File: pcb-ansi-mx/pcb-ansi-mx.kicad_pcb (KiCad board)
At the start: 2 copper layers, 200 parts, among them J1 USB_C_Receptacle_USB2.0, J2 Conn_01x04, J3 Conn_01x05, SW1 SW_Push, SW2 SW_Push, U1 XC6206PxxxMR, U2 SRV05-4, U3 RP2040, U4 W25Q128JVS, Y1 Crystal_GND24

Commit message: feat: add rotary encoder
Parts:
- added ENC1: RotaryEncoder_Switch, PCM_marbastlib-various:ROT_Alps_EC11E-Switch, F.Cu at (319.1, 23.8)

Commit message: feat: initial key matrix + encoder debounce
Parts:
- added C13: 22p, Capacitor_SMD:C_0402_1005Metric, B.Cu at (191.3, 166.3)
- added C14: 22p, Capacitor_SMD:C_0402_1005Metric, B.Cu at (191.3, 168.3)
- added D_ENC1: D_Small, Diode_SMD:D_SOD-123, B.Cu at (307.2, 23.8)
- added R10: 5k1, Resistor_SMD:R_0402_1005Metric, B.Cu at (343.2, 24.6)
- added R11: 27, Resistor_SMD:R_0402_1005Metric, B.Cu at (194.2, 165.0)
- added R12: 27, Resistor_SMD:R_0402_1005Metric, B.Cu at (194.2, 166.9)
- added R13: 1k, Resistor_SMD:R_0402_1005Metric, B.Cu at (194.2, 168.9)
- C10: value 1u -> 10n
- C11: value 22p -> 10n
- C12: value 22p -> 1u
- ENC1: moved to B.Cu
- R7, R8: value 27 -> 5k1
- R9: value 1k -> 5k1
- S1: value Backspace -> LShift; footprint PCM_marbastlib-mx:STAB_MX_P_2u -> PCM_marbastlib-mx:STAB_MX_P_2.25u; moved to B.Cu
- S2: value Enter -> Space; footprint PCM_marbastlib-mx:STAB_MX_P_2.25u -> PCM_marbastlib-mx:STAB_MX_P_6.25u; moved to B.Cu
- S3: value LShift -> Backspace; footprint PCM_marbastlib-mx:STAB_MX_P_2.25u -> PCM_marbastlib-mx:STAB_MX_P_2u; moved to B.Cu
- S4: value Space -> Enter; footprint PCM_marbastlib-mx:STAB_MX_P_6.25u -> PCM_marbastlib-mx:STAB_MX_P_2.25u; moved to B.Cu
- moved R9 329.1 mm to (346.1, 24.6)
- moved R7 328.6 mm to (346.4, 22.2)
- moved R8 327.1 mm to (343.8, 22.2)
- moved C10 265.8 mm to (353.5, 22.2)
- moved C11 265.8 mm to (353.5, 24.2)
- moved S1 252.4 mm to (34.9, 104.0), turned to 180 degrees
- moved S3 251.2 mm to (280.2, 46.8), turned to 180 degrees
- moved S2 139.2 mm to (144.5, 123.0)
- moved S4 138.1 mm to (277.8, 84.9)
- moved J1 52.2 mm to (77.3, 159.3)
- moved C1 13.9 mm to (122.8, 170.5)
- moved C2 13.9 mm to (122.8, 172.5)
- moved C3 13.9 mm to (122.8, 174.5)
- moved C4 13.9 mm to (122.8, 176.4)
- moved C5 13.9 mm to (43.4, 178.7)
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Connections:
- C10 pad 1: +3V3 -> ENC_B
- C11 pad 1: GND -> ENC_A
- C11 pad 2: XIN -> GND
- C12 pad 1: GND -> +3V3
- C12 pad 2: Net-(C12-Pad2) -> GND
- D1 pad 1: unconnected-(D1-K-Pad1) -> ROW0
- D10 pad 1: unconnected-(D10-K-Pad1) -> ROW0
- D11 pad 1: unconnected-(D11-K-Pad1) -> ROW0
- D12 pad 1: unconnected-(D12-K-Pad1) -> ROW0
- D13 pad 1: unconnected-(D13-K-Pad1) -> ROW0
- D14 pad 1: unconnected-(D14-K-Pad1) -> ROW0
- D15 pad 1: unconnected-(D15-K-Pad1) -> ROW1
- D16 pad 1: unconnected-(D16-K-Pad1) -> ROW1
- D17 pad 1: unconnected-(D17-K-Pad1) -> ROW1
- D18 pad 1: unconnected-(D18-K-Pad1) -> ROW1
- D19 pad 1: unconnected-(D19-K-Pad1) -> ROW1
- D2 pad 1: unconnected-(D2-K-Pad1) -> ROW0
- D20 pad 1: unconnected-(D20-K-Pad1) -> ROW1
- D21 pad 1: unconnected-(D21-K-Pad1) -> ROW1
- D22 pad 1: unconnected-(D22-K-Pad1) -> ROW1
- D23 pad 1: unconnected-(D23-K-Pad1) -> ROW1
- D24 pad 1: unconnected-(D24-K-Pad1) -> ROW1
- D25 pad 1: unconnected-(D25-K-Pad1) -> ROW1
- D26 pad 1: unconnected-(D26-K-Pad1) -> ROW1
- D27 pad 1: unconnected-(D27-K-Pad1) -> ROW1
- D28 pad 1: unconnected-(D28-K-Pad1) -> ROW1
- D29 pad 1: unconnected-(D29-K-Pad1) -> ROW1
- D3 pad 1: unconnected-(D3-K-Pad1) -> ROW0
- D30 pad 1: unconnected-(D30-K-Pad1) -> ROW2
- D31 pad 1: unconnected-(D31-K-Pad1) -> ROW2
- D32 pad 1: unconnected-(D32-K-Pad1) -> ROW2
- D33 pad 1: unconnected-(D33-K-Pad1) -> ROW2
- D34 pad 1: unconnected-(D34-K-Pad1) -> ROW2
- D35 pad 1: unconnected-(D35-K-Pad1) -> ROW2
- D36 pad 1: unconnected-(D36-K-Pad1) -> ROW2
- D37 pad 1: unconnected-(D37-K-Pad1) -> ROW2
- D38 pad 1: unconnected-(D38-K-Pad1) -> ROW2
- D39 pad 1: unconnected-(D39-K-Pad1) -> ROW2
- D4 pad 1: unconnected-(D4-K-Pad1) -> ROW0
- D40 pad 1: unconnected-(D40-K-Pad1) -> ROW2
- D41 pad 1: unconnected-(D41-K-Pad1) -> ROW2
- D42 pad 1: unconnected-(D42-K-Pad1) -> ROW2
- D43 pad 1: unconnected-(D43-K-Pad1) -> ROW2
- D44 pad 1: unconnected-(D44-K-Pad1) -> ROW2
- D45 pad 1: unconnected-(D45-K-Pad1) -> ROW3
- D46 pad 1: unconnected-(D46-K-Pad1) -> ROW3
- D47 pad 1: unconnected-(D47-K-Pad1) -> ROW3
- D48 pad 1: unconnected-(D48-K-Pad1) -> ROW3
- D49 pad 1: unconnected-(D49-K-Pad1) -> ROW3
- D5 pad 1: unconnected-(D5-K-Pad1) -> ROW0
- D50 pad 1: unconnected-(D50-K-Pad1) -> ROW3
- D51 pad 1: unconnected-(D51-K-Pad1) -> ROW3
- D52 pad 1: unconnected-(D52-K-Pad1) -> ROW3
- D53 pad 1: unconnected-(D53-K-Pad1) -> ROW3
- D54 pad 1: unconnected-(D54-K-Pad1) -> ROW3
- D55 pad 1: unconnected-(D55-K-Pad1) -> ROW3
- D56 pad 1: unconnected-(D56-K-Pad1) -> ROW3
- D57 pad 1: unconnected-(D57-K-Pad1) -> ROW3
- D58 pad 1: unconnected-(D58-K-Pad1) -> ROW3
- D59 pad 1: unconnected-(D59-K-Pad1) -> ROW4
- D6 pad 1: unconnected-(D6-K-Pad1) -> ROW0
- D60 pad 1: unconnected-(D60-K-Pad1) -> ROW4
- D61 pad 1: unconnected-(D61-K-Pad1) -> ROW4
- D62 pad 1: unconnected-(D62-K-Pad1) -> ROW4
- D63 pad 1: unconnected-(D63-K-Pad1) -> ROW4
- D64 pad 1: unconnected-(D64-K-Pad1) -> ROW4
- D65 pad 1: unconnected-(D65-K-Pad1) -> ROW4
- D66 pad 1: unconnected-(D66-K-Pad1) -> ROW4
- D67 pad 1: unconnected-(D67-K-Pad1) -> ROW4
- D68 pad 1: unconnected-(D68-K-Pad1) -> ROW4
- D69 pad 1: unconnected-(D69-K-Pad1) -> ROW4
- D7 pad 1: unconnected-(D7-K-Pad1) -> ROW0
- D70 pad 1: unconnected-(D70-K-Pad1) -> ROW4
- D71 pad 1: unconnected-(D71-K-Pad1) -> ROW4
- D72 pad 1: unconnected-(D72-K-Pad1) -> ROW4
- D73 pad 1: unconnected-(D73-K-Pad1) -> ROW5
- D74 pad 1: unconnected-(D74-K-Pad1) -> ROW5
- D75 pad 1: unconnected-(D75-K-Pad1) -> ROW5
- D76 pad 1: unconnected-(D76-K-Pad1) -> ROW5
- D77 pad 1: unconnected-(D77-K-Pad1) -> ROW5
- D78 pad 1: unconnected-(D78-K-Pad1) -> ROW5
- D79 pad 1: unconnected-(D79-K-Pad1) -> ROW5
- D8 pad 1: unconnected-(D8-K-Pad1) -> ROW0
- D80 pad 1: unconnected-(D80-K-Pad1) -> ROW5
- D81 pad 1: unconnected-(D81-K-Pad1) -> ROW5
- D82 pad 1: unconnected-(D82-K-Pad1) -> ROW5
- D9 pad 1: unconnected-(D9-K-Pad1) -> ROW0
- ENC1 pad A: unconnected-(ENC1-PadA) -> Net-(ENC1-PadA)
- ENC1 pad B: unconnected-(ENC1-PadB) -> Net-(ENC1-PadB)
- ENC1 pad C: unconnected-(ENC1-PadC) -> GND
- ENC1 pad S1: unconnected-(ENC1-PadS1) -> Net-(D_ENC1-A)
- ENC1 pad S2: unconnected-(ENC1-PadS2) -> COL14
- MX1 pad 1: unconnected-(MX1-Pad1) -> COL0
- MX10 pad 1: unconnected-(MX10-Pad1) -> COL9
- MX11 pad 1: unconnected-(MX11-Pad1) -> COL10
- MX12 pad 1: unconnected-(MX12-Pad1) -> COL11
- MX13 pad 1: unconnected-(MX13-Pad1) -> COL12
- MX14 pad 1: unconnected-(MX14-Pad1) -> COL13
- MX15 pad 1: unconnected-(MX15-Pad1) -> COL0
- MX16 pad 1: unconnected-(MX16-Pad1) -> COL1
- MX17 pad 1: unconnected-(MX17-Pad1) -> COL2
- MX18 pad 1: unconnected-(MX18-Pad1) -> COL3
- MX19 pad 1: unconnected-(MX19-Pad1) -> COL4
- MX2 pad 1: unconnected-(MX2-Pad1) -> COL1
- MX20 pad 1: unconnected-(MX20-Pad1) -> COL5
- MX21 pad 1: unconnected-(MX21-Pad1) -> COL6
- MX22 pad 1: unconnected-(MX22-Pad1) -> COL7
- MX23 pad 1: unconnected-(MX23-Pad1) -> COL8
- MX24 pad 1: unconnected-(MX24-Pad1) -> COL9
- MX25 pad 1: unconnected-(MX25-Pad1) -> COL10
- MX26 pad 1: unconnected-(MX26-Pad1) -> COL11
- MX27 pad 1: unconnected-(MX27-Pad1) -> COL12
- MX28 pad 1: unconnected-(MX28-Pad1) -> COL13
- MX29 pad 1: unconnected-(MX29-Pad1) -> COL14
- MX3 pad 1: unconnected-(MX3-Pad1) -> COL2
- MX30 pad 1: unconnected-(MX30-Pad1) -> COL0
- MX31 pad 1: unconnected-(MX31-Pad1) -> COL1
- MX32 pad 1: unconnected-(MX32-Pad1) -> COL2
- MX33 pad 1: unconnected-(MX33-Pad1) -> COL3
- MX34 pad 1: unconnected-(MX34-Pad1) -> COL4
- MX35 pad 1: unconnected-(MX35-Pad1) -> COL5
- MX36 pad 1: unconnected-(MX36-Pad1) -> COL6
- MX37 pad 1: unconnected-(MX37-Pad1) -> COL7
- MX38 pad 1: unconnected-(MX38-Pad1) -> COL8
- MX39 pad 1: unconnected-(MX39-Pad1) -> COL9
- MX4 pad 1: unconnected-(MX4-Pad1) -> COL3
- MX40 pad 1: unconnected-(MX40-Pad1) -> COL10
- MX41 pad 1: unconnected-(MX41-Pad1) -> COL11
- MX42 pad 1: unconnected-(MX42-Pad1) -> COL12
- MX43 pad 1: unconnected-(MX43-Pad1) -> COL13
- MX44 pad 1: unconnected-(MX44-Pad1) -> COL14
- MX45 pad 1: unconnected-(MX45-Pad1) -> COL0
- MX46 pad 1: unconnected-(MX46-Pad1) -> COL1
- MX47 pad 1: unconnected-(MX47-Pad1) -> COL2
- MX48 pad 1: unconnected-(MX48-Pad1) -> COL3
- MX49 pad 1: unconnected-(MX49-Pad1) -> COL4
- MX5 pad 1: unconnected-(MX5-Pad1) -> COL4
- MX50 pad 1: unconnected-(MX50-Pad1) -> COL5
- MX51 pad 1: unconnected-(MX51-Pad1) -> COL6
- MX52 pad 1: unconnected-(MX52-Pad1) -> COL7
- MX53 pad 1: unconnected-(MX53-Pad1) -> COL8
- MX54 pad 1: unconnected-(MX54-Pad1) -> COL9
- MX55 pad 1: unconnected-(MX55-Pad1) -> COL10
- MX56 pad 1: unconnected-(MX56-Pad1) -> COL11
- MX57 pad 1: unconnected-(MX57-Pad1) -> COL12
- MX58 pad 1: unconnected-(MX58-Pad1) -> COL14
- MX59 pad 1: unconnected-(MX59-Pad1) -> COL0
- MX6 pad 1: unconnected-(MX6-Pad1) -> COL5
- MX60 pad 1: unconnected-(MX60-Pad1) -> COL1
- MX61 pad 1: unconnected-(MX61-Pad1) -> COL2
- MX62 pad 1: unconnected-(MX62-Pad1) -> COL3
- MX63 pad 1: unconnected-(MX63-Pad1) -> COL4
- MX64 pad 1: unconnected-(MX64-Pad1) -> COL5
- MX65 pad 1: unconnected-(MX65-Pad1) -> COL6
- MX66 pad 1: unconnected-(MX66-Pad1) -> COL7
- MX67 pad 1: unconnected-(MX67-Pad1) -> COL8
- MX68 pad 1: unconnected-(MX68-Pad1) -> COL9
- MX69 pad 1: unconnected-(MX69-Pad1) -> COL10
- MX7 pad 1: unconnected-(MX7-Pad1) -> COL6
- MX70 pad 1: unconnected-(MX70-Pad1) -> COL11
- MX71 pad 1: unconnected-(MX71-Pad1) -> COL12
- MX72 pad 1: unconnected-(MX72-Pad1) -> COL14
- MX73 pad 1: unconnected-(MX73-Pad1) -> COL0
- MX74 pad 1: unconnected-(MX74-Pad1) -> COL1
- MX75 pad 1: unconnected-(MX75-Pad1) -> COL2
- MX76 pad 1: unconnected-(MX76-Pad1) -> COL5
- MX77 pad 1: unconnected-(MX77-Pad1) -> COL8
- MX78 pad 1: unconnected-(MX78-Pad1) -> COL9
- MX79 pad 1: unconnected-(MX79-Pad1) -> COL10
- MX8 pad 1: unconnected-(MX8-Pad1) -> COL7
- MX80 pad 1: unconnected-(MX80-Pad1) -> COL11
- MX81 pad 1: unconnected-(MX81-Pad1) -> COL12
- MX82 pad 1: unconnected-(MX82-Pad1) -> COL13
- MX9 pad 1: unconnected-(MX9-Pad1) -> COL8
- R7 pad 1: D+ -> Net-(R7-Pad1)
- R7 pad 2: Net-(U3-USB_DP) -> Net-(ENC1-PadA)
- R8 pad 1: D- -> ENC_A
- R8 pad 2: Net-(U3-USB_DM) -> Net-(R7-Pad1)
- R9 pad 1: Net-(C12-Pad2) -> Net-(R10-Pad2)
- R9 pad 2: XOUT -> Net-(ENC1-PadB)
- Y1 pad 1: Net-(C12-Pad2) -> Net-(C14-Pad2)

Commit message: refactor: remove f13 (to make space for usb port)
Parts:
- removed D82: D_Small, Diode_SMD:D_SOD-123
- removed MX82: MX_SW_HS, PCM_marbastlib-mx:SW_MX_HS_1u
- MX29, MX42: footprint PCM_marbastlib-mx:SW_MX_HS_1u -> PCM_marbastlib-mx:SW_MX_HS_1.5u
- MX30, MX43: footprint PCM_marbastlib-mx:SW_MX_HS_1.5u -> PCM_marbastlib-mx:SW_MX_HS_1u
- MX44, MX69: footprint PCM_marbastlib-mx:SW_MX_HS_1u -> PCM_marbastlib-mx:SW_MX_HS_1.75u
- MX45, MX70: footprint PCM_marbastlib-mx:SW_MX_HS_1.75u -> PCM_marbastlib-mx:SW_MX_HS_1u
- MX72: footprint PCM_marbastlib-mx:SW_MX_HS_1u -> PCM_marbastlib-mx:SW_MX_HS_1.25u
- MX75: footprint PCM_marbastlib-mx:SW_MX_HS_1.25u -> PCM_marbastlib-mx:SW_MX_HS_1u
- moved MX29 291.1 mm to (27.8, 65.9)
- moved D29 291.1 mm to (31.0, 66.7)
- moved MX44 288.8 mm to (30.2, 84.9)
- moved D44 288.8 mm to (33.3, 85.7)
- moved MX58 284.0 mm to (34.9, 104.0)
- moved D58 284.0 mm to (38.1, 104.8)
- moved MX72 269.5 mm to (25.4, 123.0)
- moved D72 269.5 mm to (28.6, 123.8)
- moved MX14 267.8 mm to (23.0, 46.8)
- moved D14 267.8 mm to (26.2, 47.6)
- moved J1 145.4 mm to (42.1, 18.3)
- moved D75 71.4 mm to (147.6, 123.8)
- moved MX75 71.4 mm to (144.5, 123.0)
- moved D76 69.1 mm to (216.7, 123.8)
- moved MX76 69.1 mm to (213.5, 123.0)
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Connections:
- D14 pad 1: ROW0 -> ROW1
- D29 pad 1: ROW1 -> ROW2
- D44 pad 1: ROW2 -> ROW3
- D58 pad 1: ROW3 -> ROW4
- D72 pad 1: ROW4 -> ROW5
- MX14 pad 1: COL13 -> COL0
- MX15 pad 1: COL0 -> COL1
- MX16 pad 1: COL1 -> COL2
- MX17 pad 1: COL2 -> COL3
- MX18 pad 1: COL3 -> COL4
- MX19 pad 1: COL4 -> COL5
- MX20 pad 1: COL5 -> COL6
- MX21 pad 1: COL6 -> COL7
- MX22 pad 1: COL7 -> COL8
- MX23 pad 1: COL8 -> COL9
- MX24 pad 1: COL9 -> COL10
- MX25 pad 1: COL10 -> COL11
- MX26 pad 1: COL11 -> COL12
- MX27 pad 1: COL12 -> COL13
- MX28 pad 1: COL13 -> COL14
- MX29 pad 1: COL14 -> COL0
- MX30 pad 1: COL0 -> COL1
- MX31 pad 1: COL1 -> COL2
- MX32 pad 1: COL2 -> COL3
- MX33 pad 1: COL3 -> COL4
- MX34 pad 1: COL4 -> COL5
- MX35 pad 1: COL5 -> COL6
- MX36 pad 1: COL6 -> COL7
- MX37 pad 1: COL7 -> COL8
- MX38 pad 1: COL8 -> COL9
- MX39 pad 1: COL9 -> COL10
- MX40 pad 1: COL10 -> COL11
- MX41 pad 1: COL11 -> COL12
- MX42 pad 1: COL12 -> COL13
- MX43 pad 1: COL13 -> COL14
- MX44 pad 1: COL14 -> COL0
- MX45 pad 1: COL0 -> COL1
- MX46 pad 1: COL1 -> COL2
- MX47 pad 1: COL2 -> COL3
- MX48 pad 1: COL3 -> COL4
- MX49 pad 1: COL4 -> COL5
- MX50 pad 1: COL5 -> COL6
- MX51 pad 1: COL6 -> COL7
- MX52 pad 1: COL7 -> COL8
- MX53 pad 1: COL8 -> COL9
- MX54 pad 1: COL9 -> COL10
- MX55 pad 1: COL10 -> COL11
- MX56 pad 1: COL11 -> COL12
- MX57 pad 1: COL12 -> COL14
- MX58 pad 1: COL14 -> COL0
- MX59 pad 1: COL0 -> COL1
- MX60 pad 1: COL1 -> COL2
- MX61 pad 1: COL2 -> COL3
- MX62 pad 1: COL3 -> COL4
- MX63 pad 1: COL4 -> COL5
- MX64 pad 1: COL5 -> COL6
- MX65 pad 1: COL6 -> COL7
- MX66 pad 1: COL7 -> COL8
- MX67 pad 1: COL8 -> COL9
- MX68 pad 1: COL9 -> COL10
- MX69 pad 1: COL10 -> COL11
- MX70 pad 1: COL11 -> COL12
- MX71 pad 1: COL12 -> COL14
- MX72 pad 1: COL14 -> COL0
- MX73 pad 1: COL0 -> COL1
- MX74 pad 1: COL1 -> COL2
- MX75 pad 1: COL2 -> COL5
- MX76 pad 1: COL5 -> COL8
- MX77 pad 1: COL8 -> COL9
- MX78 pad 1: COL9 -> COL10
- MX79 pad 1: COL10 -> COL11
- MX80 pad 1: COL11 -> COL12
- MX81 pad 1: COL12 -> COL13

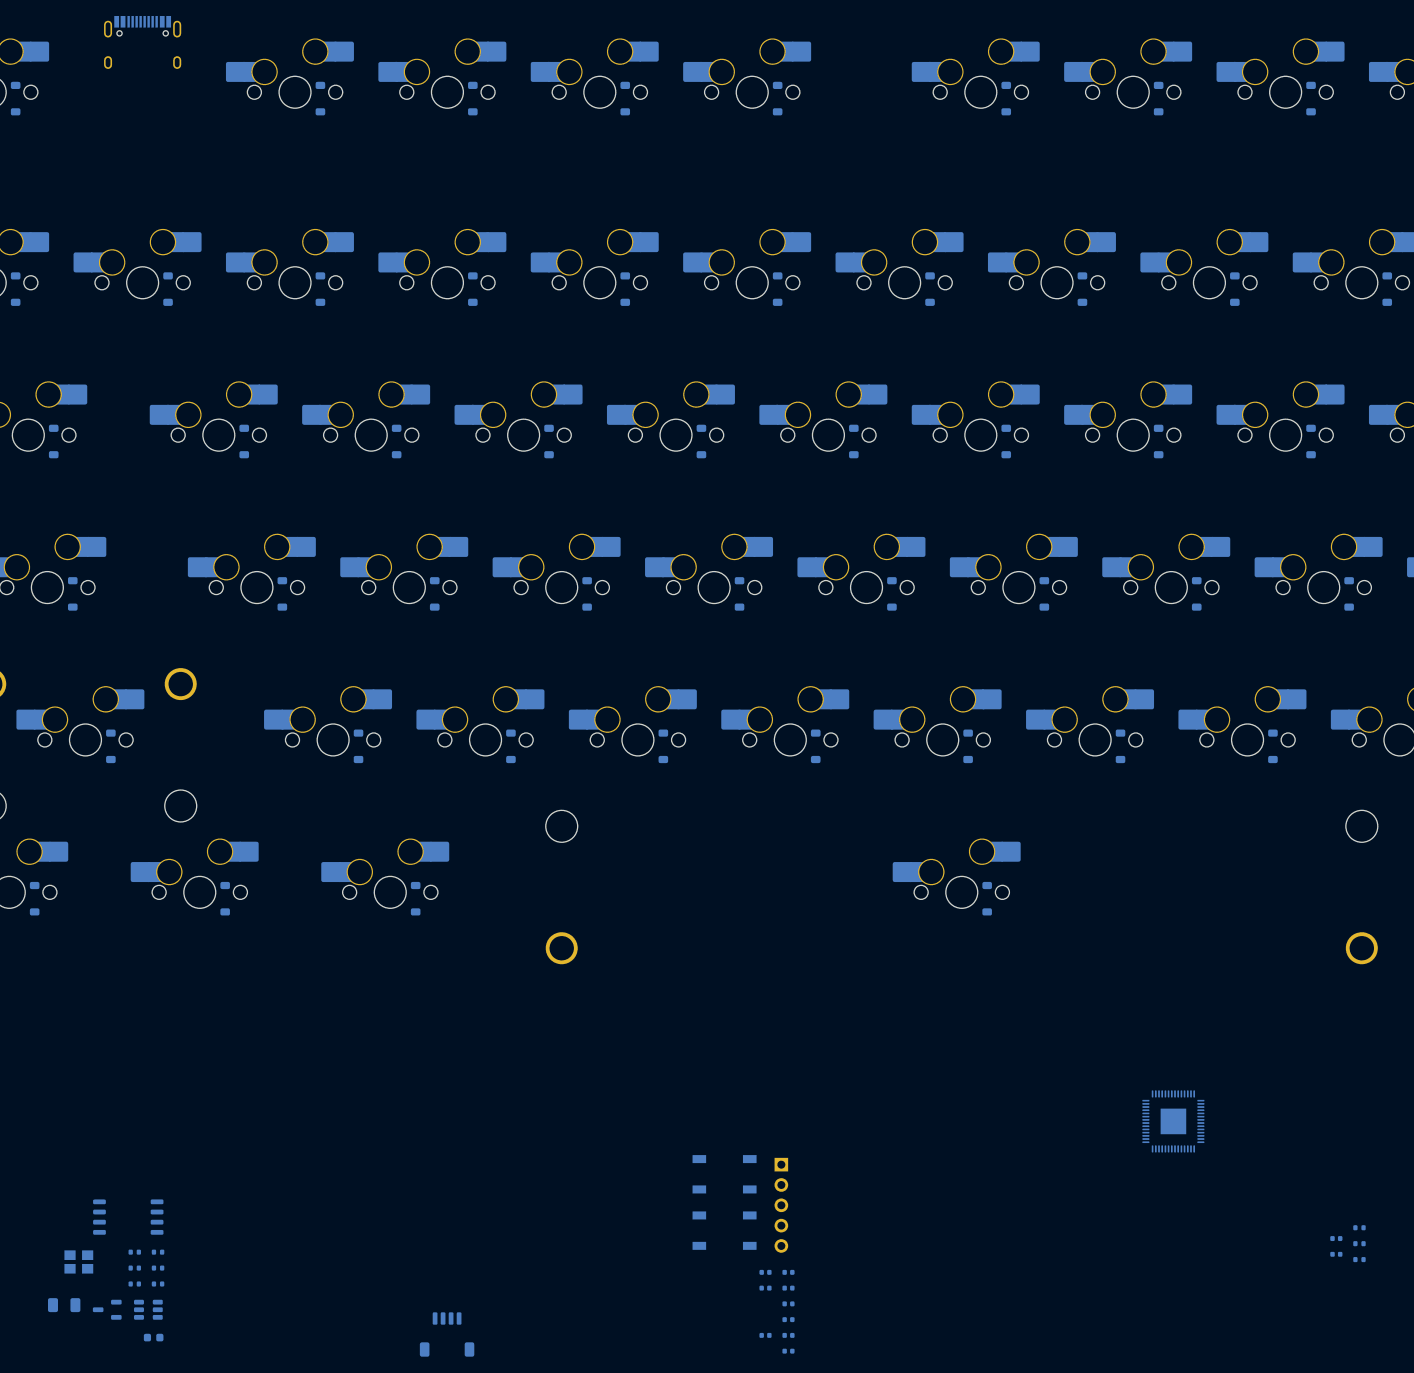
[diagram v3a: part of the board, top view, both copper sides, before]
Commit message: refactor: use molex instead of jst for daughterboard connector
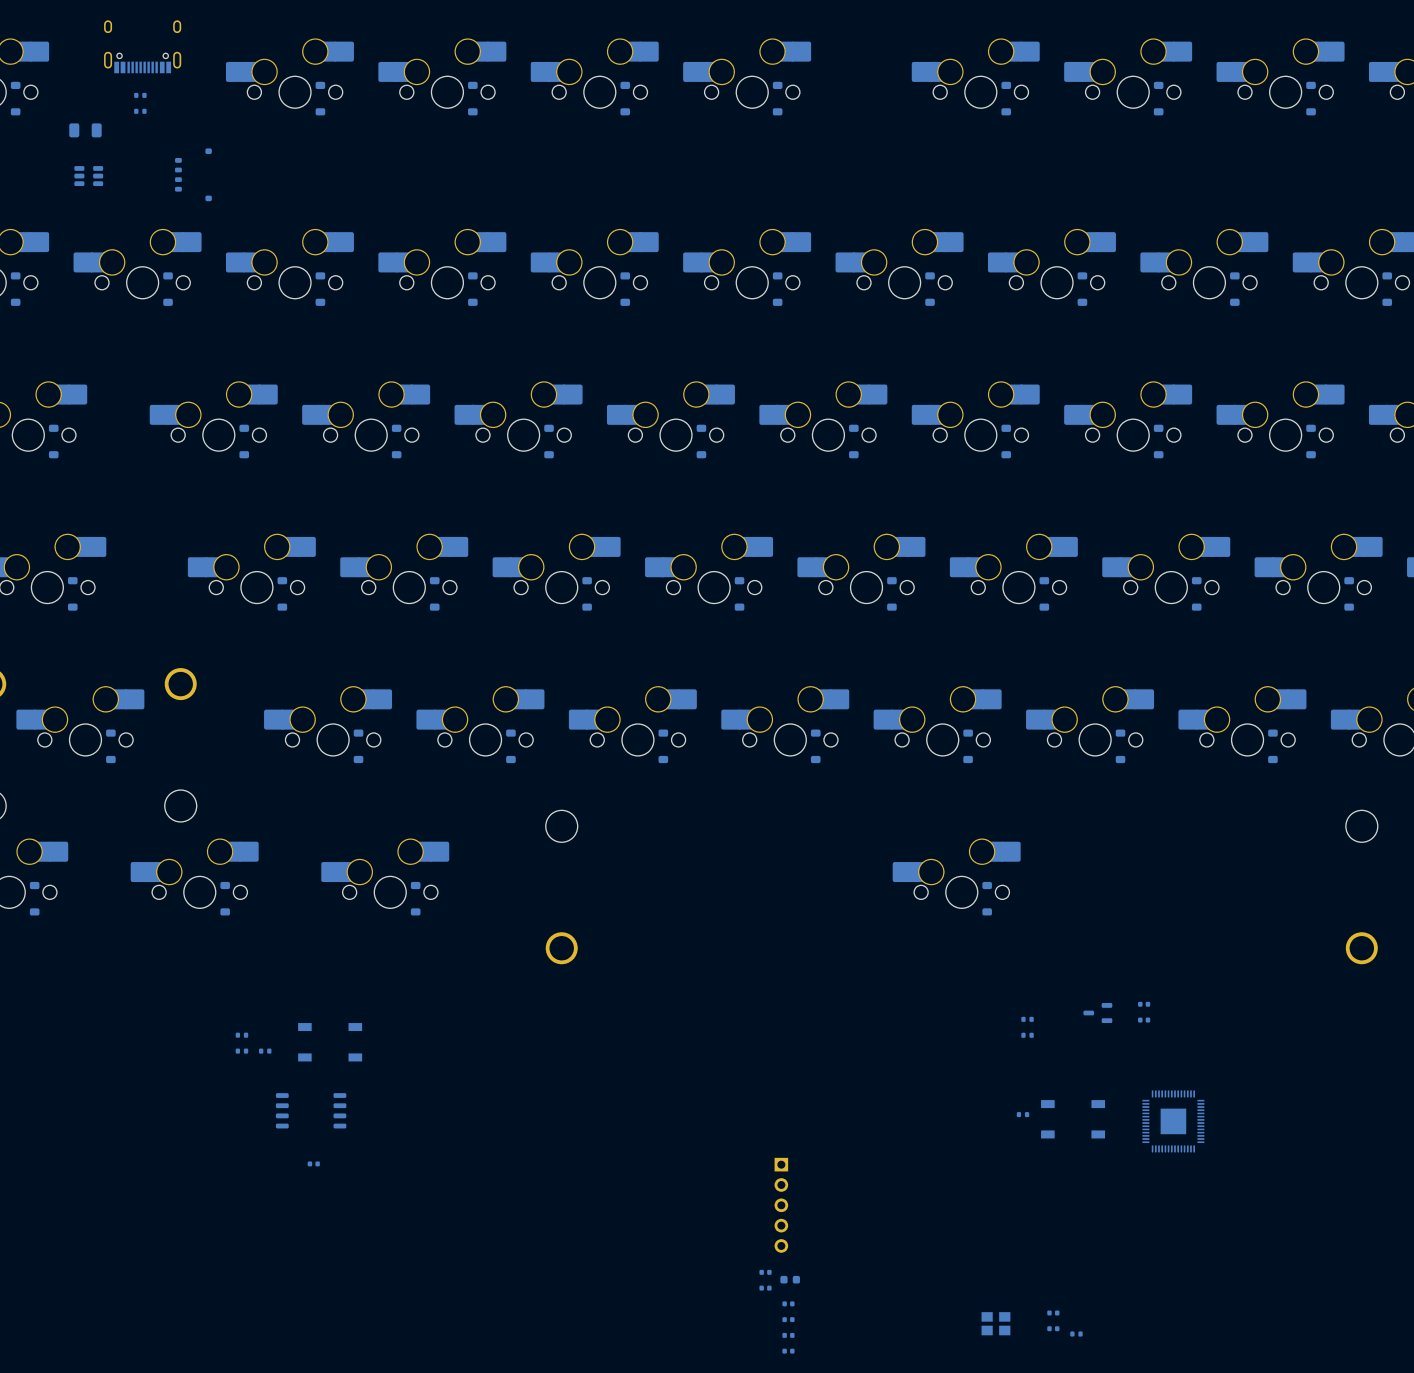
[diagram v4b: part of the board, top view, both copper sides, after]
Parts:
- J2: footprint Connector_JST:JST_SH_SM04B-SRSS-TB_1x04-1MP_P1.00mm_Horizontal -> Connector_Molex:Molex_Pico-EZmate_78171-0004_1x04-1MP_P1.20mm_Vertical
- moved J2 148.4 mm to (48.4, 33.3), turned to -90 degrees
- moved F1 146.9 mm to (34.9, 27.8)
- moved R1 144.6 mm to (41.8, 23.4)
- moved R2 144.6 mm to (41.8, 25.4)
- moved U2 141.9 mm to (35.3, 33.5)
- moved U1 129.3 mm to (161.5, 138.1)
- moved Y1 114.9 mm to (148.7, 176.9)
- moved R4 112.4 mm to (152.1, 150.8)
- moved C5 79.9 mm to (123.0, 171.4)
- moved C12 60.4 mm to (63.5, 157.0)
- moved C1 55.7 mm to (167.3, 137.0)
- moved C2 55.7 mm to (167.3, 139.0)
- moved SW2 54.6 mm to (65.5, 141.8)
- moved R11 49.0 mm to (152.7, 138.9)
- moved R12 49.0 mm to (152.7, 140.9)
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
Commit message: refactor: remove daughterboard connector
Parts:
- removed J2: Conn_01x04, Connector_Molex:Molex_Pico-EZmate_78171-0004_1x04-1MP_P1.20mm_Vertical
- added C15: 10n, Capacitor_SMD:C_0402_1005Metric, B.Cu at (330.5, 26.2)
- added C16: 1u, Capacitor_SMD:C_0402_1005Metric, B.Cu at (183.7, 138.1)
- added C17: 22p, Capacitor_SMD:C_0402_1005Metric, B.Cu at (172.6, 166.3)
- added C18: 22p, Capacitor_SMD:C_0402_1005Metric, B.Cu at (168.7, 166.3)
- C10, C11: value 10n -> 100n
- C12: value 1u -> 100n
- C13: value 22p -> 100n
- C14: value 22p -> 10n
- C5: value 10u -> 100n; footprint Capacitor_SMD:C_0603_1608Metric -> Capacitor_SMD:C_0402_1005Metric
- C6: value 1u -> 10u; footprint Capacitor_SMD:C_0402_1005Metric -> Capacitor_SMD:C_0603_1608Metric
- C7: value 100n -> 1u
- moved C14 233.6 mm to (331.4, 23.5), turned to 135 degrees
- moved C11 202.7 mm to (171.3, 146.0), turned to 90 degrees
- moved C10 201.7 mm to (176.7, 149.2), turned to 0 degrees
- moved R5 138.1 mm to (192.6, 142.1)
- moved R6 138.1 mm to (192.6, 144.1)
- moved SW2 138.1 mm to (203.6, 143.0)
- moved R3 138.1 mm to (195.5, 144.1)
- moved U4 117.3 mm to (180.2, 142.9)
- moved C12 107.1 mm to (170.6, 158.0), turned to -90 degrees
- moved C9 60.1 mm to (176.5, 152.4), turned to 0 degrees
- moved C5 55.4 mm to (172.2, 146.0), turned to 90 degrees
- moved C3 54.6 mm to (169.4, 146.0), turned to 90 degrees
- moved C6 54.5 mm to (161.9, 140.5)
- moved C7 52.1 mm to (164.6, 149.2)
- moved C4 50.1 mm to (169.4, 158.0), turned to -90 degrees
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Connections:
- C10 pad 1: ENC_B -> +3V3
- C11 pad 1: ENC_A -> +3V3
- C13 pad 1: GND -> +3V3
- C13 pad 2: XIN -> GND
- C14 pad 1: GND -> ENC_B
- C14 pad 2: Net-(C14-Pad2) -> GND
- C5 pad 1: +3V3 -> +1V1
- R13 pad 1: Net-(C14-Pad2) -> Net-(C18-Pad2)
- Y1 pad 1: Net-(C14-Pad2) -> Net-(C18-Pad2)
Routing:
- net D+: track 0.00 -> 3.19 mm
- net D-: track 0.00 -> 3.10 mm
- net Net-(J1-CC1): track 0.00 -> 2.77 mm
- net Net-(J1-CC2): track 0.00 -> 2.57 mm

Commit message: feat: route everything but encoder and matrix
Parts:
- ENC1: moved to F.Cu
- moved SW2 77.8 mm to (144.4, 92.6)
- moved R3 77.4 mm to (138.9, 91.3), turned to 0 degrees
- moved R6 73.1 mm to (138.9, 94.5)
- moved R5 72.8 mm to (138.9, 92.9)
- moved C1 70.4 mm to (102.7, 93.7), turned to 180 degrees
- moved U1 69.1 mm to (107.2, 95.2)
- moved C2 68.4 mm to (110.3, 95.2)
- moved C16 65.0 mm to (126.2, 107.9)
- moved C13 64.8 mm to (115.6, 111.2)
- moved C3 63.2 mm to (116.6, 111.2)
- moved C11 62.7 mm to (119.6, 110.6)
- moved C5 62.7 mm to (120.6, 110.6)
- moved R12 62.2 mm to (118.2, 108.6)
- moved R11 62.2 mm to (119.2, 108.6)
- moved R13 62.2 mm to (119.0, 125.8)
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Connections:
- J3 pad 1: RESET -> SWC
- J3 pad 2: +3V3 -> SWD
- J3 pad 3: GND -> RESET
- J3 pad 4: SWC -> +3V3
- J3 pad 5: SWD -> GND
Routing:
- net D+: track 3.19 -> 158.1 mm
- net D-: track 3.10 -> 156.5 mm
- net +3V3: track 0.00 -> 134.6 mm, vias 0 -> 4
- net +5V: track 0.00 -> 132.3 mm
- net GND: track 0.00 -> 129.8 mm, vias 0 -> 24
- net Q_SEL: track 0.00 -> 45.6 mm
- net +1V1: track 0.00 -> 29.6 mm, vias 0 -> 3
- net RESET: track 0.00 -> 28.8 mm
- net Q_IO1: track 0.00 -> 21.7 mm
- net Q_IO2: track 0.00 -> 20.1 mm
- net VBUS: track 0.00 -> 14.5 mm
- net SWD: track 0.00 -> 13.3 mm
- net SWC: track 0.00 -> 12.5 mm
- net Q_IO3: track 0.00 -> 11.8 mm
- net Q_CLK: track 0.00 -> 10.8 mm
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- added copper zone on B.Cu, net GND
- added copper zone on F.Cu, net GND
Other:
- board outline added: 314.3 x 123 mm
